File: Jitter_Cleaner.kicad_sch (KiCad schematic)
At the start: 49 parts, among them T1 TCM2-43X+, T3 TCM2-43X+, U18 SI5394, U20 TLV75733PDBV, U21 TLV75718PDBV, U23 74AVC4T245, U26 74LVC8T245, Y1 CX3225SB48000D0FPJC1

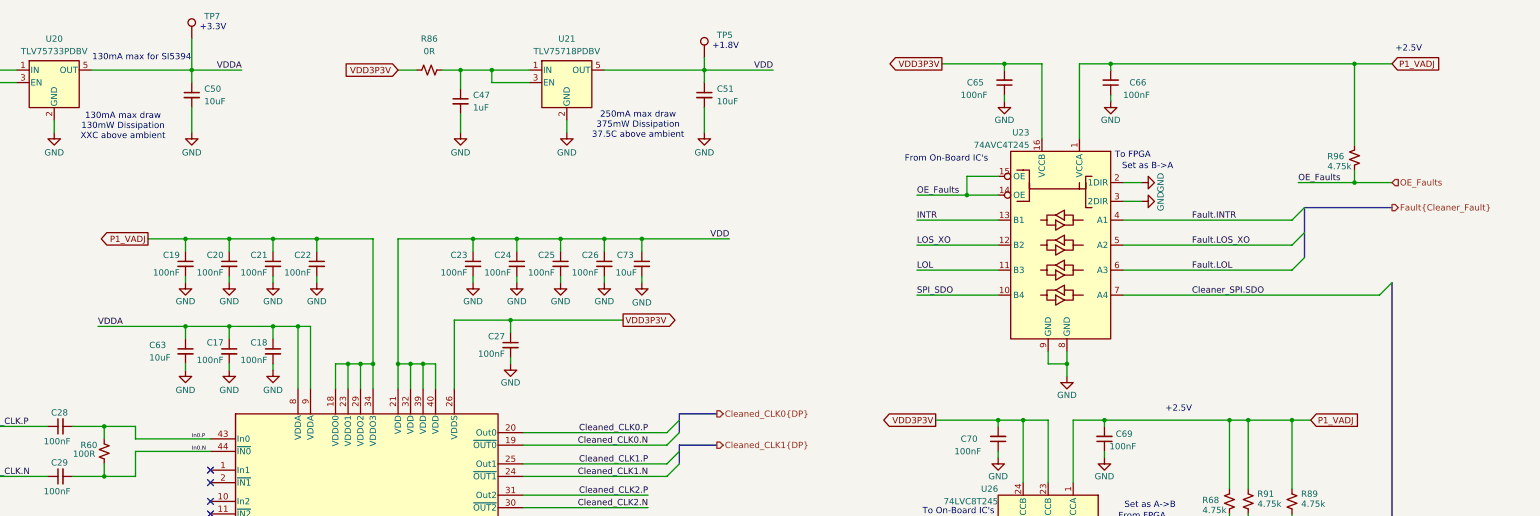
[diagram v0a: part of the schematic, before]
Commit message: Final Draft - Ready for review
Updates:
- Changed area behind FMC connector to match the new Osprey FMC template
  - This includes a new 12V LED, more robust power input traces, arranged elements for readability.

Things to do:
Round diff traces before generating fabrication files
Change name of project to 'trigger output fmc'
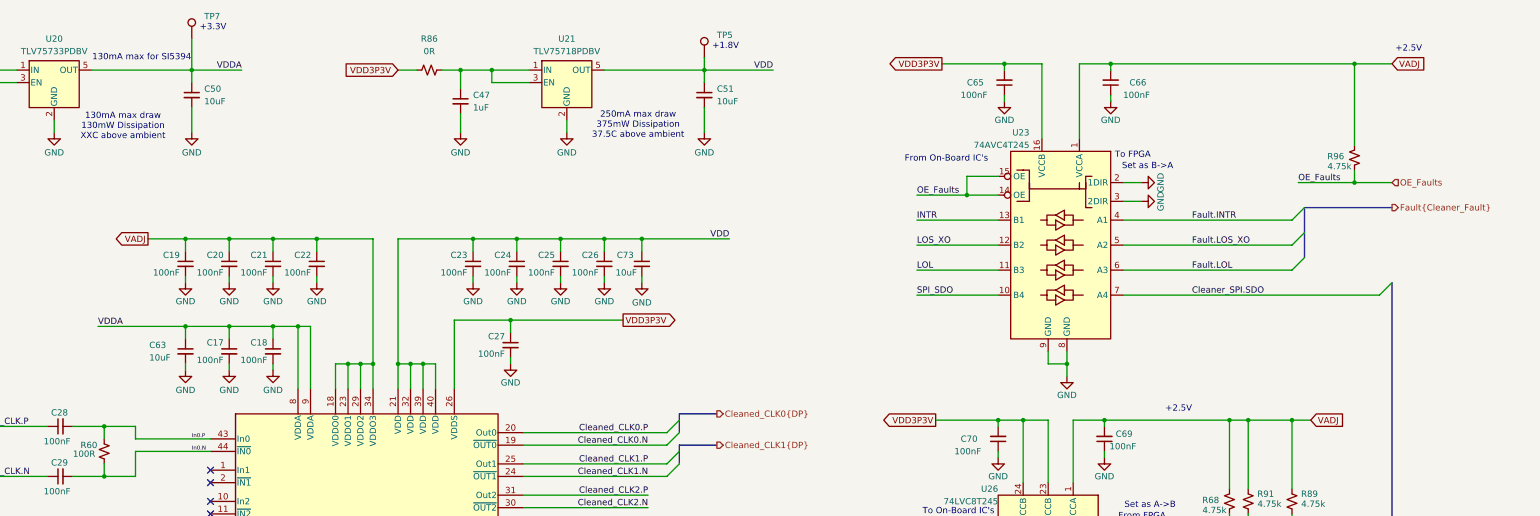
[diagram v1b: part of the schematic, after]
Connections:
- net P1_VADJ renamed VADJ
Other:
- title: FMC Template -> Trigger Output FMC
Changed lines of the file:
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@@
 	(paper "A3")
 	(title_block
-		(title "FMC Template")
-		(date "2026-01-26")
+		(title "Trigger Output FMC")
+		(date "2026-05-07")
 		(rev "1.0")
 		(company "SPDX-FileCopyrightText: 2025 Osprey DCS")
@@
 		)
 	)
-	(global_label "P1_VADJ"
+	(global_label "VADJ"
 		(shape input)
 		(at 349.25 121.92 0)
@@
 		)
 		(property "Intersheetrefs" "${INTERSHEET_REFS}"
-			(at 360.0971 121.92 0)
+			(at 356.65 121.92 0)
 			(effects
 				(font
@@
 		)
 	)
-	(global_label "P1_VADJ"
+	(global_label "VADJ"
 		(shape output)
 		(at 113.03 85.09 180)
@@
 		)
 		(property "Intersheetrefs" "${INTERSHEET_REFS}"
-			(at 102.1829 85.09 0)
+			(at 105.63 85.09 0)
 			(effects
 				(font
@@
 		)
 	)
-	(global_label "P1_VADJ"
+	(global_label "VADJ"
 		(shape input)
 		(at 365.76 49.53 0)
@@
 		)
 		(property "Intersheetrefs" "${INTERSHEET_REFS}"
-			(at 376.6071 49.53 0)
+			(at 373.16 49.53 0)
 			(effects
 				(font

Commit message: Changed Trigger Outputs Topology
- Changed to a comp to digital TX design
- Added power section to support this change
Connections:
- net GND: no longer U26.10 (A8), U26.6 (A4), U26.9 (A7)
- no-connect marks 11 -> 14
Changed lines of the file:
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@@
 	)
 	(no_connect
+		(at 308.61 163.83)
+	)
+	(no_connect
 		(at 125.73 140.97)
 	)
 	(no_connect
+		(at 308.61 184.15)
+	)
+	(no_connect
 		(at 125.73 144.78)
 	)
@@
 		(at 125.73 138.43)
 	)
+	(no_connect
+		(at 308.61 179.07)
+	)
 	(bus_entry
 		(at 67.31 125.73)
@@
 	(wire
 		(pts
+			(xy 71.12 48.26) (xy 71.12 50.8)
+		)
+		(stroke
+			(width 0)
+			(type default)
+		)
+	)
+	(wire
+		(pts
 			(xy 187.96 85.09) (xy 187.96 87.63)
 		)
@@
 	(wire
 		(pts
-			(xy 308.61 184.15) (xy 312.42 184.15)
-		)
-		(stroke
-			(width 0)
-			(type default)
-		)
-	)
-	(wire
-		(pts
 			(xy 287.02 49.53) (xy 287.02 50.8)
 		)
@@
 	(wire
 		(pts
-			(xy 308.61 163.83) (xy 312.42 163.83)
-		)
-		(stroke
-			(width 0)
-			(type default)
-		)
-	)
-	(wire
-		(pts
 			(xy 300.99 134.62) (xy 300.99 121.92)
 		)
@@
 	(wire
 		(pts
-			(xy 308.61 179.07) (xy 312.42 179.07)
-		)
-		(stroke
-			(width 0)
-			(type default)
-		)
-	)
-	(wire
-		(pts
 			(xy 193.04 212.09) (xy 193.04 217.17)
 		)
@@
 	(wire
 		(pts
+			(xy 176.53 48.26) (xy 176.53 50.8)
+		)
+		(stroke
+			(width 0)
+			(type default)
+		)
+	)
+	(wire
+		(pts
 			(xy 186.69 101.6) (xy 186.69 104.14)
 		)
@@
 	)
 	(symbol
-		(lib_id "power:GND")
-		(at 312.42 163.83 90)
-		(mirror x)
-		(unit 1)
-		(exclude_from_sim no)
-		(in_bom yes)
-		(on_board yes)
-		(dnp no)
-		(property "Reference" "#PWR0124"
-			(at 318.77 163.83 0)
-			(effects
-				(font
-					(size 1.27 1.27)
-				)
-				(hide yes)
-			)
-		)
-		(property "Value" "GND"
-			(at 311.15 162.56 90)
-			(effects
-				(font
-					(size 1.27 1.27)
-				)
-			)
-		)
-		(property "Footprint" ""
-			(at 312.42 163.83 0)
-			(effects
-				(font
-					(size 1.27 1.27)
-				)
-				(hide yes)
-			)
-		)
-		(property "Datasheet" ""
-			(at 312.42 163.83 0)
-			(effects
-				(font
-					(size 1.27 1.27)
-				)
-				(hide yes)
-			)
-		)
-		(property "Description" ""
-			(at 312.42 163.83 0)
-			(effects
-				(font
-					(size 1.27 1.27)
-				)
-				(hide yes)
-			)
-		)
-		(pin "1"
-		)
-		(instances
-			(project "evr-fmc"
-				(path "/1719e569-47c8-4fa0-8523-9c9686ef0dba/51b6ba02-2a45-47f9-920d-b1129f765b02"
-					(reference "#PWR0129")
-					(unit 1)
-				)
-				(path "/1719e569-47c8-4fa0-8523-9c9686ef0dba/72a6e05f-9d23-47d7-93ac-d48e996d2022"
-					(reference "#PWR0124")
-					(unit 1)
-				)
-			)
-		)
-	)
-	(symbol
 		(lib_id "Device:C_Small")
 		(at 186.69 106.68 0)
@@
 	)
 	(symbol
-		(lib_id "power:GND")
-		(at 312.42 179.07 90)
-		(mirror x)
-		(unit 1)
-		(exclude_from_sim no)
-		(in_bom yes)
-		(on_board yes)
-		(dnp no)
-		(property "Reference" "#PWR0105"
-			(at 318.77 179.07 0)
-			(effects
-				(font
-					(size 1.27 1.27)
-				)
-				(hide yes)
-			)
-		)
-		(property "Value" "GND"
-			(at 311.15 177.8 90)
-			(effects
-				(font
-					(size 1.27 1.27)
-				)
-			)
-		)
-		(property "Footprint" ""
-			(at 312.42 179.07 0)
-			(effects
-				(font
-					(size 1.27 1.27)
-				)
-				(hide yes)
-			)
-		)
-		(property "Datasheet" ""
-			(at 312.42 179.07 0)
-			(effects
-				(font
-					(size 1.27 1.27)
-				)
-				(hide yes)
-			)
-		)
-		(property "Description" ""
-			(at 312.42 179.07 0)
-			(effects
-				(font
-					(size 1.27 1.27)
-				)
-				(hide yes)
-			)
-		)
-		(pin "1"
-		)
-		(instances
-			(project "evr-fmc"
-				(path "/1719e569-47c8-4fa0-8523-9c9686ef0dba/51b6ba02-2a45-47f9-920d-b1129f765b02"
-					(reference "#PWR0106")
-					(unit 1)
-				)
-				(path "/1719e569-47c8-4fa0-8523-9c9686ef0dba/72a6e05f-9d23-47d7-93ac-d48e996d2022"
-					(reference "#PWR0105")
-					(unit 1)
-				)
-			)
-		)
-	)
-	(symbol
 		(lib_id "Device:C_Small")
 		(at 153.67 212.09 90)
@@
 	)
 	(symbol
+		(lib_id "power:PWR_FLAG")
+		(at 71.12 48.26 0)
+		(mirror y)
+		(unit 1)
+		(exclude_from_sim no)
+		(in_bom yes)
+		(on_board yes)
+		(dnp no)
+		(fields_autoplaced yes)
+		(property "Reference" "#FLG03"
+			(at 71.12 46.355 0)
+			(effects
+				(font
+					(size 1.27 1.27)
+				)
+				(hide yes)
+			)
+		)
+		(property "Value" "PWR_FLAG"
+			(at 71.12 43.18 0)
+			(effects
+				(font
+					(size 1.27 1.27)
+				)
+			)
+		)
+		(property "Footprint" ""
+			(at 71.12 48.26 0)
+			(effects
+				(font
+					(size 1.27 1.27)
+				)
+				(hide yes)
+			)
+		)
+		(property "Datasheet" "~"
+			(at 71.12 48.26 0)
+			(effects
+				(font
+					(size 1.27 1.27)
+				)
+				(hide yes)
+			)
+		)
+		(property "Description" "Special symbol for telling ERC where power comes from"
+			(at 71.12 48.26 0)
+			(effects
+				(font
+					(size 1.27 1.27)
+				)
+				(hide yes)
+			)
+		)
+		(pin "1"
+		)
+		(instances
+			(project "evr-fmc"
+				(path "/1719e569-47c8-4fa0-8523-9c9686ef0dba/51b6ba02-2a45-47f9-920d-b1129f765b02"
+					(reference "#FLG04")
+					(unit 1)
+				)
+				(path "/1719e569-47c8-4fa0-8523-9c9686ef0dba/72a6e05f-9d23-47d7-93ac-d48e996d2022"
+					(reference "#FLG03")
+					(unit 1)
+				)
+			)
+		)
+	)
+	(symbol
 		(lib_id "power:GND")
 		(at 160.02 181.61 0)
@@
 	)
 	(symbol
+		(lib_id "power:PWR_FLAG")
+		(at 176.53 48.26 0)
+		(mirror y)
+		(unit 1)
+		(exclude_from_sim no)
+		(in_bom yes)
+		(on_board yes)
+		(dnp no)
+		(fields_autoplaced yes)
+		(property "Reference" "#FLG05"
+			(at 176.53 46.355 0)
+			(effects
+				(font
+					(size 1.27 1.27)
+				)
+				(hide yes)
+			)
+		)
+		(property "Value" "PWR_FLAG"
+			(at 176.53 43.18 0)
+			(effects
+				(font
+					(size 1.27 1.27)
+				)
+			)
+		)
+		(property "Footprint" ""
+			(at 176.53 48.26 0)
+			(effects
+				(font
+					(size 1.27 1.27)
+				)
+				(hide yes)
+			)
+		)
+		(property "Datasheet" "~"
+			(at 176.53 48.26 0)
+			(effects
+				(font
+					(size 1.27 1.27)
+				)
+				(hide yes)
+			)
+		)
+		(property "Description" "Special symbol for telling ERC where power comes from"
+			(at 176.53 48.26 0)
+			(effects
+				(font
+					(size 1.27 1.27)
+				)
+				(hide yes)
+			)
+		)
+		(pin "1"
+		)
+		(instances
+			(project "evr-fmc"
+				(path "/1719e569-47c8-4fa0-8523-9c9686ef0dba/51b6ba02-2a45-47f9-920d-b1129f765b02"
+					(reference "#FLG011")
+					(unit 1)
+				)
+				(path "/1719e569-47c8-4fa0-8523-9c9686ef0dba/72a6e05f-9d23-47d7-93ac-d48e996d2022"
+					(reference "#FLG05")
+					(unit 1)
+				)
+			)
+		)
+	)
+	(symbol
 		(lib_id "power:GND")
 		(at 314.96 77.47 90)
@@
 					(unit 1)
 				)
-			)
-		)
-	)
-	(symbol
-		(lib_id "power:GND")
-		(at 312.42 184.15 90)
-		(mirror x)
-		(unit 1)
-		(exclude_from_sim no)
-		(in_bom yes)
-		(on_board yes)
-		(dnp no)
-		(property "Reference" "#PWR0107"
-			(at 318.77 184.15 0)
-			(effects
-				(font
-					(size 1.27 1.27)
-				)
-				(hide yes)
-			)
-		)
-		(property "Value" "GND"
-			(at 311.15 182.88 90)
-			(effects
-				(font
-					(size 1.27 1.27)
-				)
-			)
-		)
-		(property "Footprint" ""
-			(at 312.42 184.15 0)
-			(effects
-				(font
-					(size 1.27 1.27)
-				)
-				(hide yes)
-			)
-		)
-		(property "Datasheet" ""
-			(at 312.42 184.15 0)
-			(effects
-				(font
-					(size 1.27 1.27)
-				)
-				(hide yes)
-			)
-		)
-		(property "Description" ""
-			(at 312.42 184.15 0)
-			(effects
-				(font
-					(size 1.27 1.27)
-				)
-				(hide yes)
-			)
-		)
-		(pin "1"
-		)
-		(instances
-			(project "evr-fmc"
-				(path "/1719e569-47c8-4fa0-8523-9c9686ef0dba/51b6ba02-2a45-47f9-920d-b1129f765b02"
-					(reference "#PWR0108")
-					(unit 1)
-				)
-				(path "/1719e569-47c8-4fa0-8523-9c9686ef0dba/72a6e05f-9d23-47d7-93ac-d48e996d2022"
-					(reference "#PWR0107")
-					(unit 1)
-				)

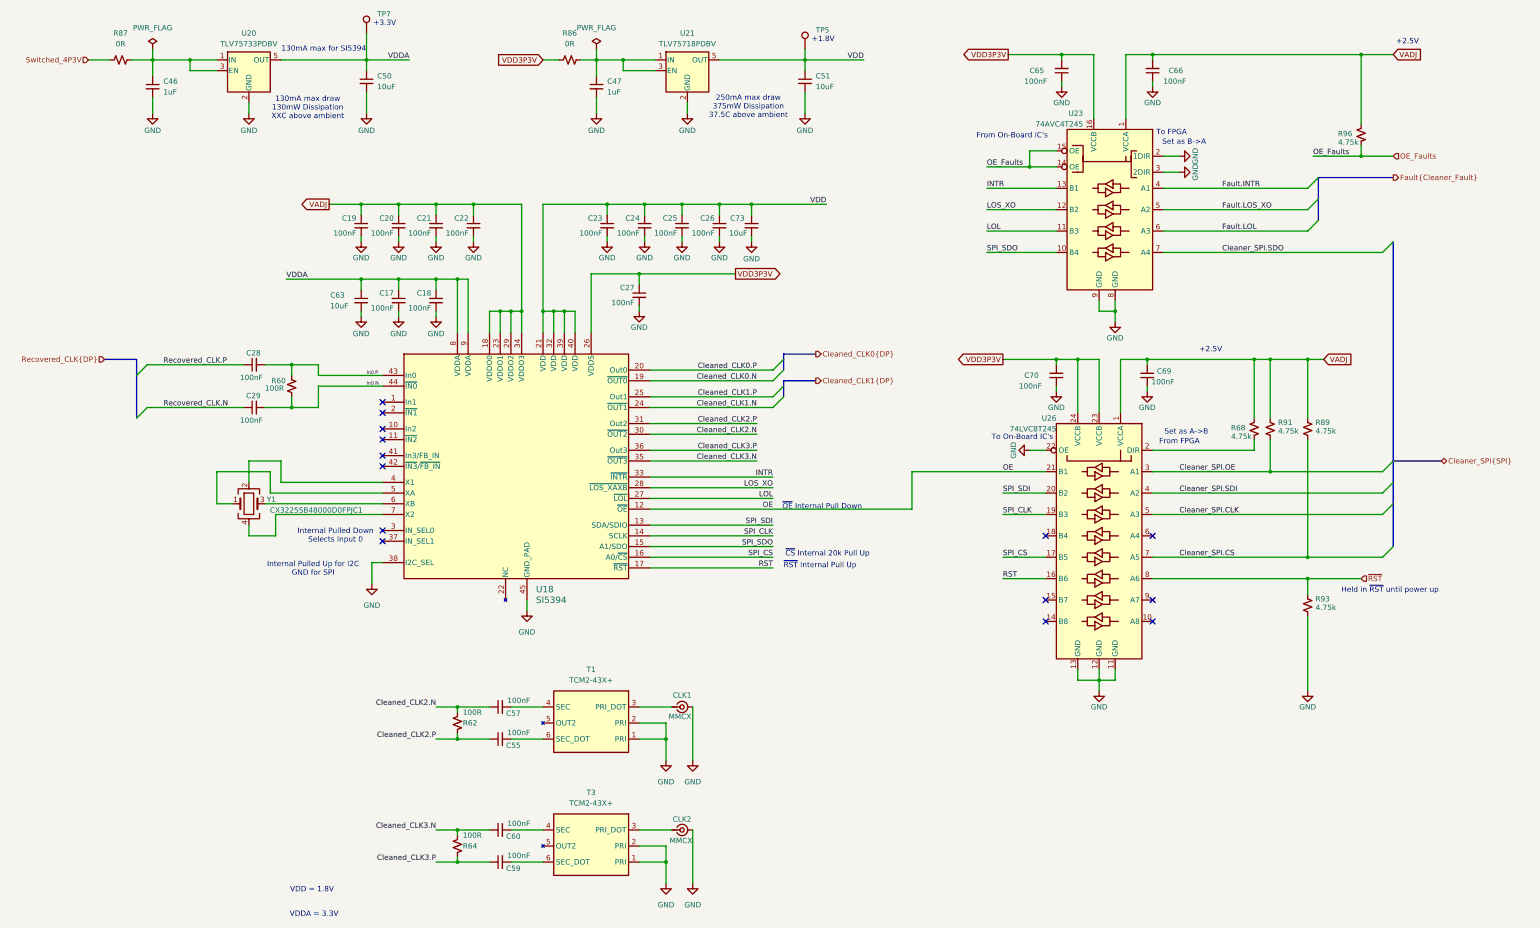
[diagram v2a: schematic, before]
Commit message: Added Level Shifter schematic & moved symbols
- Created a separate Level Shifter schematic to prepare use of some gates for Digital output enables.
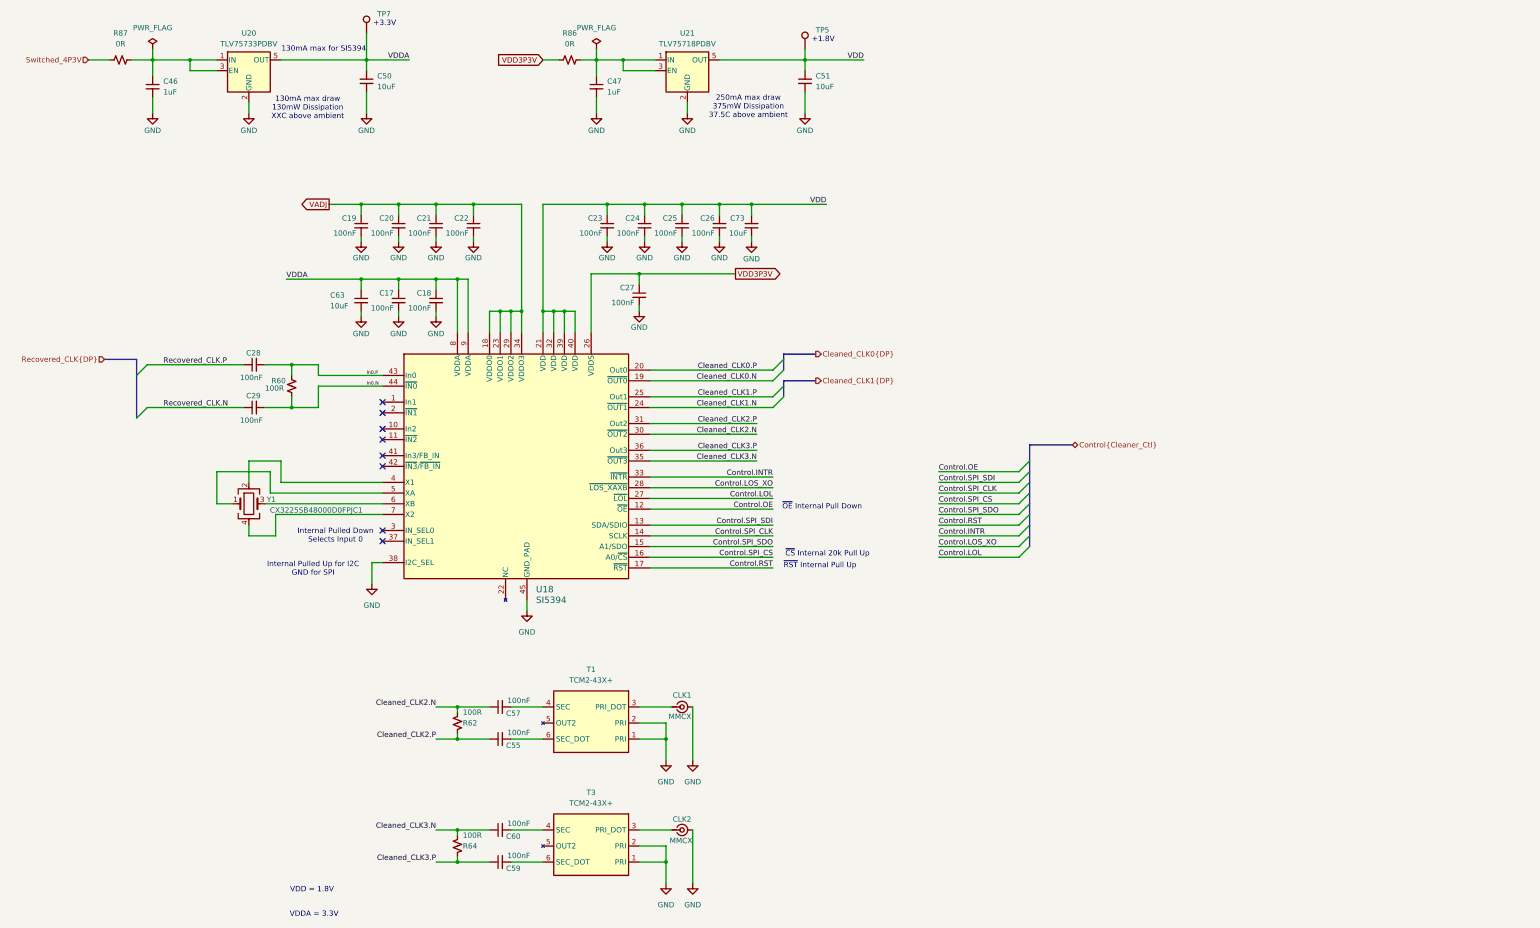
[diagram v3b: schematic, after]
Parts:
- removed C65, C66, C69, C70: 100nF, Capacitor_SMD:C_0402_1005Metric, symbol Device:C_Small
- removed R68, R89, R91, R93, R96: 4.75k, Resistor_SMD:R_0402_1005Metric, symbol Device:R_Small_US
- removed U23: 74AVC4T245, Package_SO:TSSOP-16_4.4x5mm_P0.65mm, symbol evr-fmc:74LVC4T245
- removed U26: 74LVC8T245, Package_SO:TSSOP-24_4.4x7.8mm_P0.65mm, symbol evr-fmc:74LVC8T245
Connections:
- net INTR renamed Control.INTR
- net LOL renamed Control.LOL
- net LOS_XO renamed Control.LOS_XO
- net OE renamed Control.OE
- net RST renamed Control.RST
- net SPI_CLK renamed Control.SPI_CLK
- net SPI_CS renamed Control.SPI_CS
- net SPI_SDI renamed Control.SPI_SDI
- net SPI_SDO renamed Control.SPI_SDO
- no-connect marks 14 -> 8
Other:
- note removed: "+2.5V"
- note removed: "From FPGA"
- note removed: "From On-Board IC's"
- note removed: "Held in ~{RST} until power up"
- note removed: "Set as A->B"
- note removed: "Set as B->A"
- note removed: "To FPGA"
- note removed: "To On-Board IC's"
